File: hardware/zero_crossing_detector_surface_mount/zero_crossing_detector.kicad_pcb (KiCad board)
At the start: 2 copper layers, 93 x 61 mm, 103 parts, among them J1 Conn_01x02, J2 BOOT0, J3 Conn_02x15_Odd_Even, J4 USB_B_Micro, J6 K-Type, J7 BOOT1, Q1 2N3904, Q2 2N3904, Q3 2N3904, SW1 Reset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

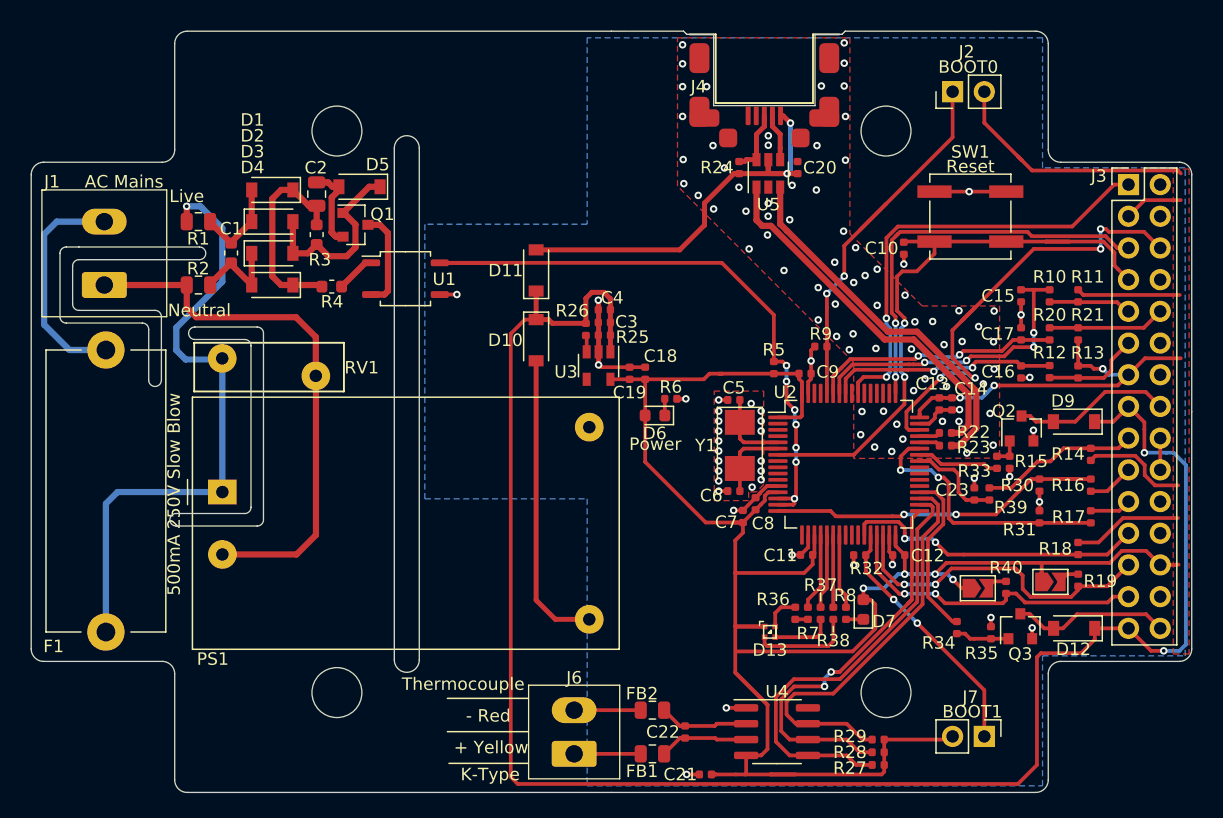
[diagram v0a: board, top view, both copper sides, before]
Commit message: Shuffled board around to put AC/DC right on the edge so hopefully it will fit alongside an SSR mounted in the lid of the box
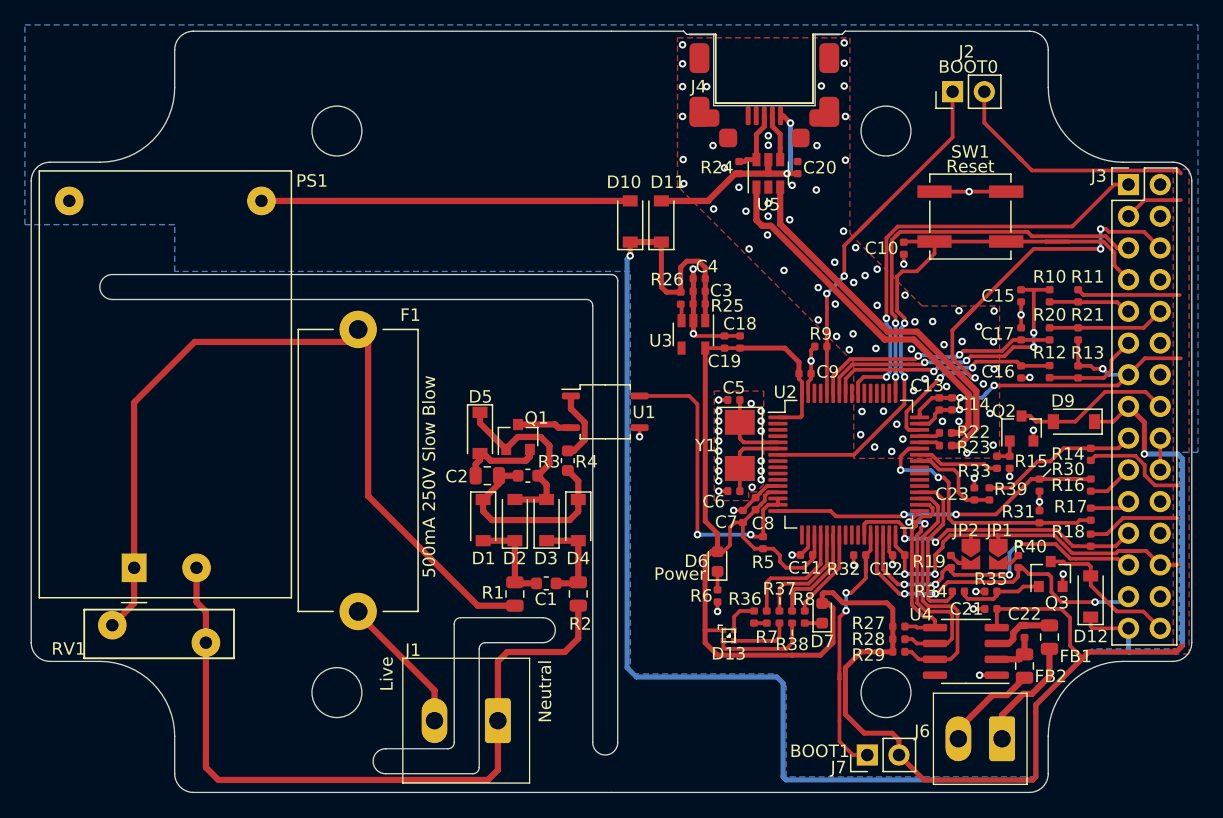
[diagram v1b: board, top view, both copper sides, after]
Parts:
- JP1, JP2: footprint Jumper:SolderJumper-2_P1.3mm_Open_TrianglePad1.0x1.5mm -> Custom:SolderJumper-2_P1.3mm_Open_TrianglePad1.0x1.5mm
- moved J1 47.0 mm to (200.9, 94.8), turned to 180 degrees
- moved R2 39.2 mm to (207.3, 84.6), turned to 270 degrees
- moved R1 39.2 mm to (202.3, 84.6), turned to 270 degrees
- moved REF** 37.8 mm to (169.8, 71.5), turned to 180 degrees
- moved C1 36.6 mm to (204.8, 83.8), turned to 0 degrees
- moved J6 34.3 mm to (241.3, 96.2), turned to 180 degrees
- moved FB1 33.2 mm to (245.1, 88.1), turned to 90 degrees
- moved D1 31.4 mm to (199.7, 78.7), turned to 270 degrees
- moved D4 30.9 mm to (207.3, 78.7), turned to 270 degrees
- moved D2 30.8 mm to (202.3, 78.7), turned to 90 degrees
- moved D3 30.7 mm to (204.8, 78.7), turned to 90 degrees
- moved FB2 30.0 mm to (243.1, 90.4), turned to 90 degrees
- moved F1 29.1 mm to (189.7, 86.0), turned to 90 degrees
- moved C22 28.4 mm to (243.1, 87.6), turned to 270 degrees
- moved C21 26.4 mm to (240.4, 85.8)
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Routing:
- net /ZC_OUT: track 51.6 -> 24.5 mm, vias 7 -> 2
- net /MAX_SCK: track 35.8 -> 15.4 mm
- net /Fused_LIVE: track 50.7 -> 67.1 mm, vias 1 -> 0
- net VCC: track 241.6 -> 257.3 mm, vias 7 -> 5
- net /NEUTRAL: track 43.7 -> 59.0 mm
- net /MAX_NSS: track 32.3 -> 18.7 mm
- net /MAX_MISO: track 33.0 -> 21.0 mm
- net /LIVE: track 18.3 -> 9.95 mm
- net /5V_USB: track 31.9 -> 24.2 mm
- net /5V_MAINS: track 24.1 -> 29.6 mm
- net Net-(FB1-Pad1): track 5.33 -> 9.19 mm
- net Net-(Q1-Pad3): track 7.99 -> 4.34 mm
- net /T-: track 7.17 -> 3.74 mm
- net /R_LED: track 6.21 -> 9.55 mm
- net /G_LED: track 5.79 -> 8.79 mm
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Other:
- outline, holes or cut-outs redrawn
- board text added: "Zero Crossing SSR Controller (SMD) v0.3 oshthings.com/zcssr 28-Jan-2020"
- board text removed: "+ Yellow"
- board text removed: "- Red"
- board text removed: "AC Mains"
- board text removed: "Zero Crossing SSR Controller (SMD) v0.2 oshthings.com/zcssr 15-Nov-19"

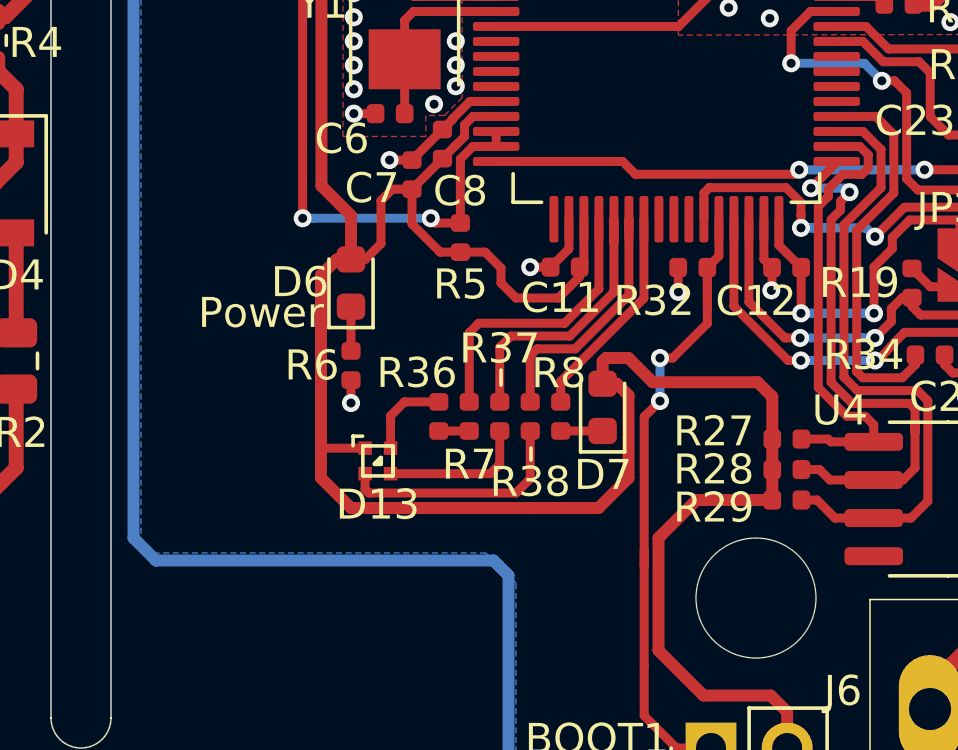
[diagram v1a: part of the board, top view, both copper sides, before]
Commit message: Removed RGB led
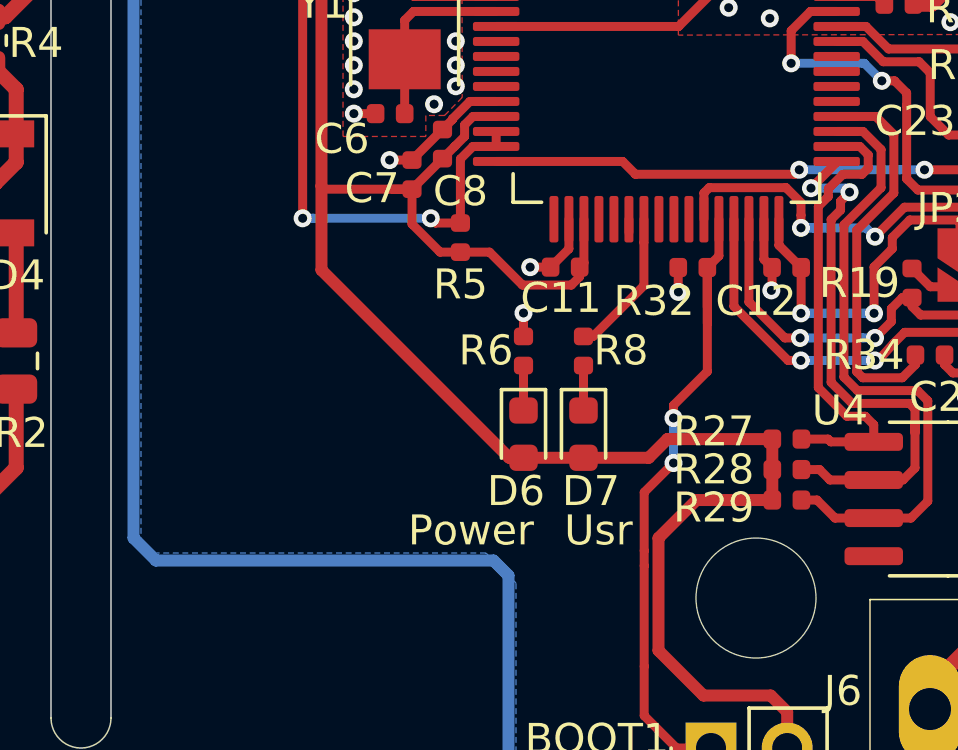
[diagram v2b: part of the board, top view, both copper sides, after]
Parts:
- removed D13: LED_ARBG, Custom:SMLP34RGB
- removed R36: 220, Resistor_SMD:R_0402_1005Metric
- removed R37: 75, Resistor_SMD:R_0402_1005Metric
- removed R38: 47, Resistor_SMD:R_0402_1005Metric
- removed R7: 33, Resistor_SMD:R_0402_1005Metric
- moved D6 7.64 mm to (224.2, 87.0), turned to 270 degrees
- moved R6 5.77 mm to (224.2, 84.3), turned to 90 degrees
- moved R8 2.31 mm to (226.2, 84.3)
- moved D7 1.10 mm to (226.2, 87.0), turned to 270 degrees
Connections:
- U2 pad 20: /R_LED -> Net-(U2-Pad20)
- U2 pad 21: /B_LED -> Net-(U2-Pad21)
- U2 pad 22: /G_LED -> Net-(U2-Pad22)
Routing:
- net VCC: track 257.3 -> 241.6 mm
- net /B_LED: track 9.59 -> 0.00 mm
- net /R_LED: track 9.55 -> 0.00 mm
- net /G_LED: track 8.79 -> 0.00 mm
- net Net-(D13-Pad4): track 7.87 -> 0.00 mm
- net Net-(D13-Pad3): track 4.88 -> 0.00 mm
- net Net-(D13-Pad2): track 2.88 -> 0.00 mm
- net /USR_LED: track 7.24 -> 4.93 mm
- net Net-(R36-Pad2): track 1.02 -> 0.00 mm
- net /BOOT1: track 22.3 -> 23.1 mm
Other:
- board text added: "Usr"
